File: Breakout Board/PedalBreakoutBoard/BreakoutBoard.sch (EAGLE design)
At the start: 7 parts, among them J1 POWER_JACK, U1 ES_DAISY_SEED_REV4, X1 5566-8, X2 5566-6

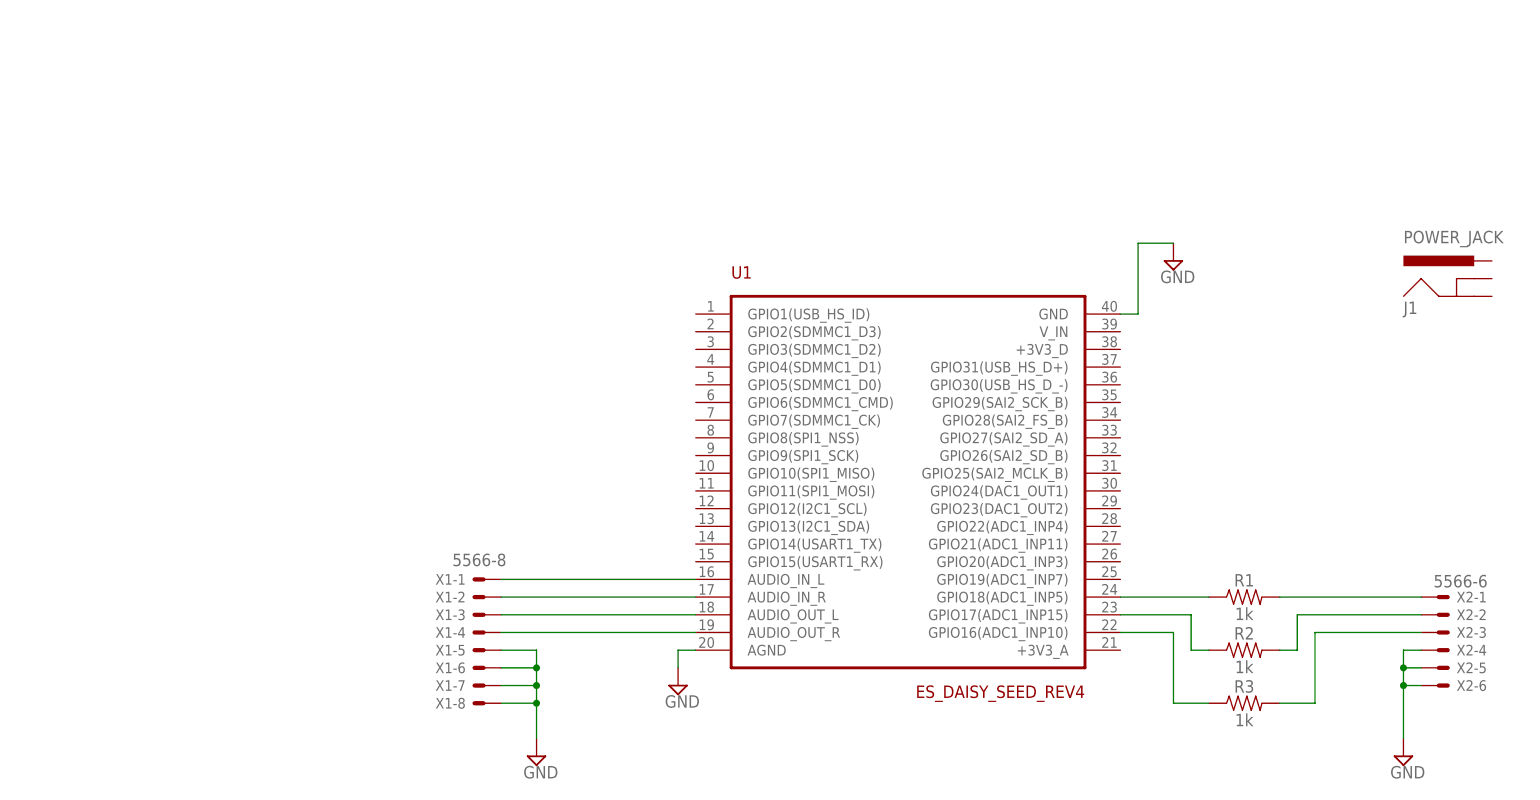
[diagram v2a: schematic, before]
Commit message: DP-16 - Add SPST molex
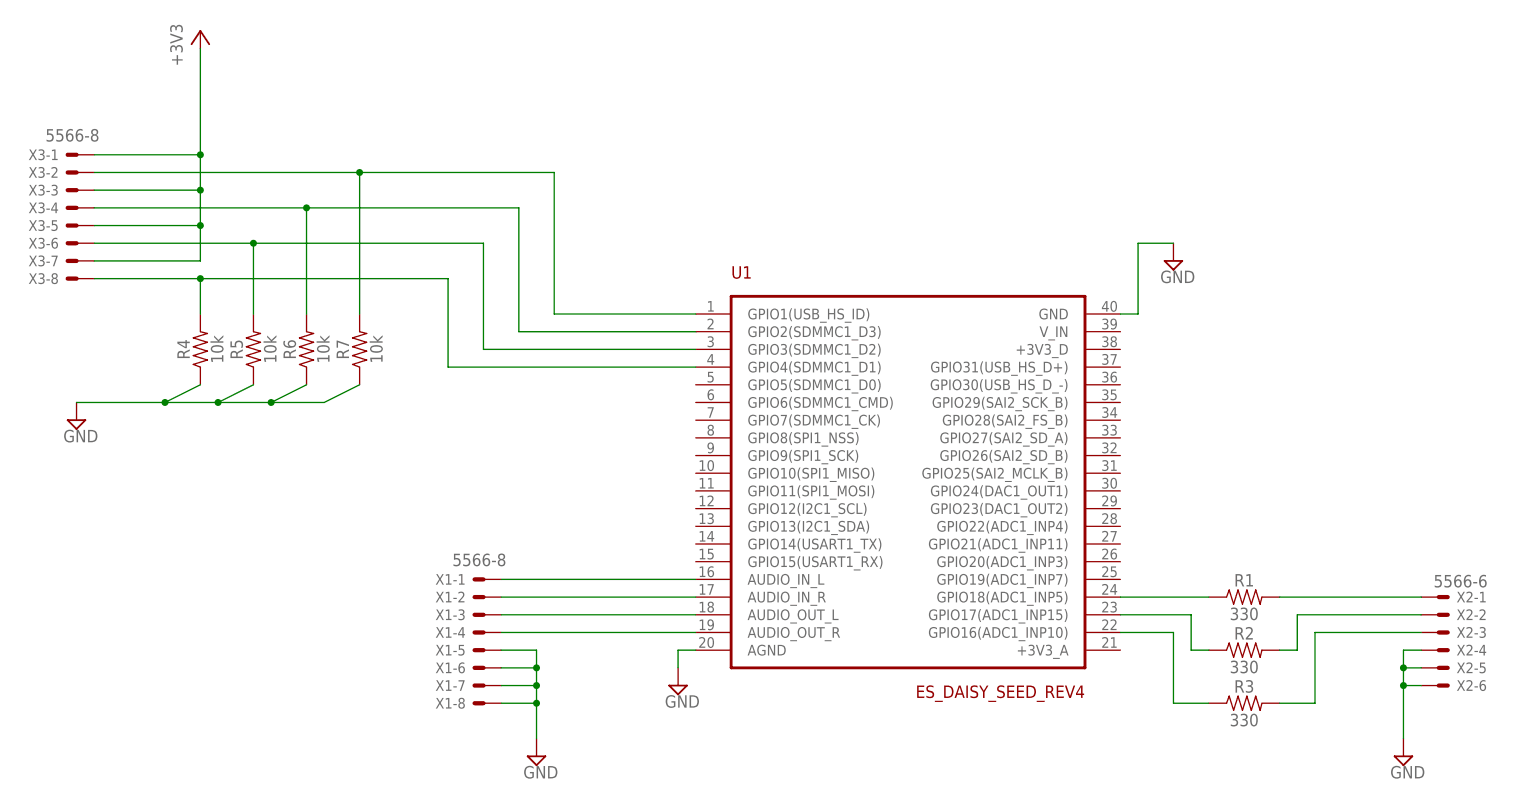
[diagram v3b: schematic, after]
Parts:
- removed J1: POWER_JACK, SparkFun-Connectors:POWER_JACK
- added R4, R5, R6, R7: 10k, SparkFun-Resistors:10KOHM-HORIZ-1/4W-5%
- added X3: 5566-8, con-molex:5566-8
- R1, R2, R3: value 1k -> 330; device SparkFun-Resistors:1KOHM-HORIZ-1/4W-5% -> SparkFun-Resistors:330OHM-HORIZ-1/10W-5%
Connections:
- new net +3V3: X3-1.S, X3-3.S, X3-5.S, X3-7.S
- new net SPST1: R7.2, U1.GPIO1(USB_HS_ID), X3-2.S
- new net SPST2: R6.2, U1.GPIO2(SDMMC1_D3), X3-4.S
- new net SPST3: R5.2, U1.GPIO3(SDMMC1_D2), X3-6.S
- new net SPST4: R4.2, U1.GPIO4(SDMMC1_D1), X3-8.S
- net GND: now also R4.1, R5.1, R6.1, R7.1

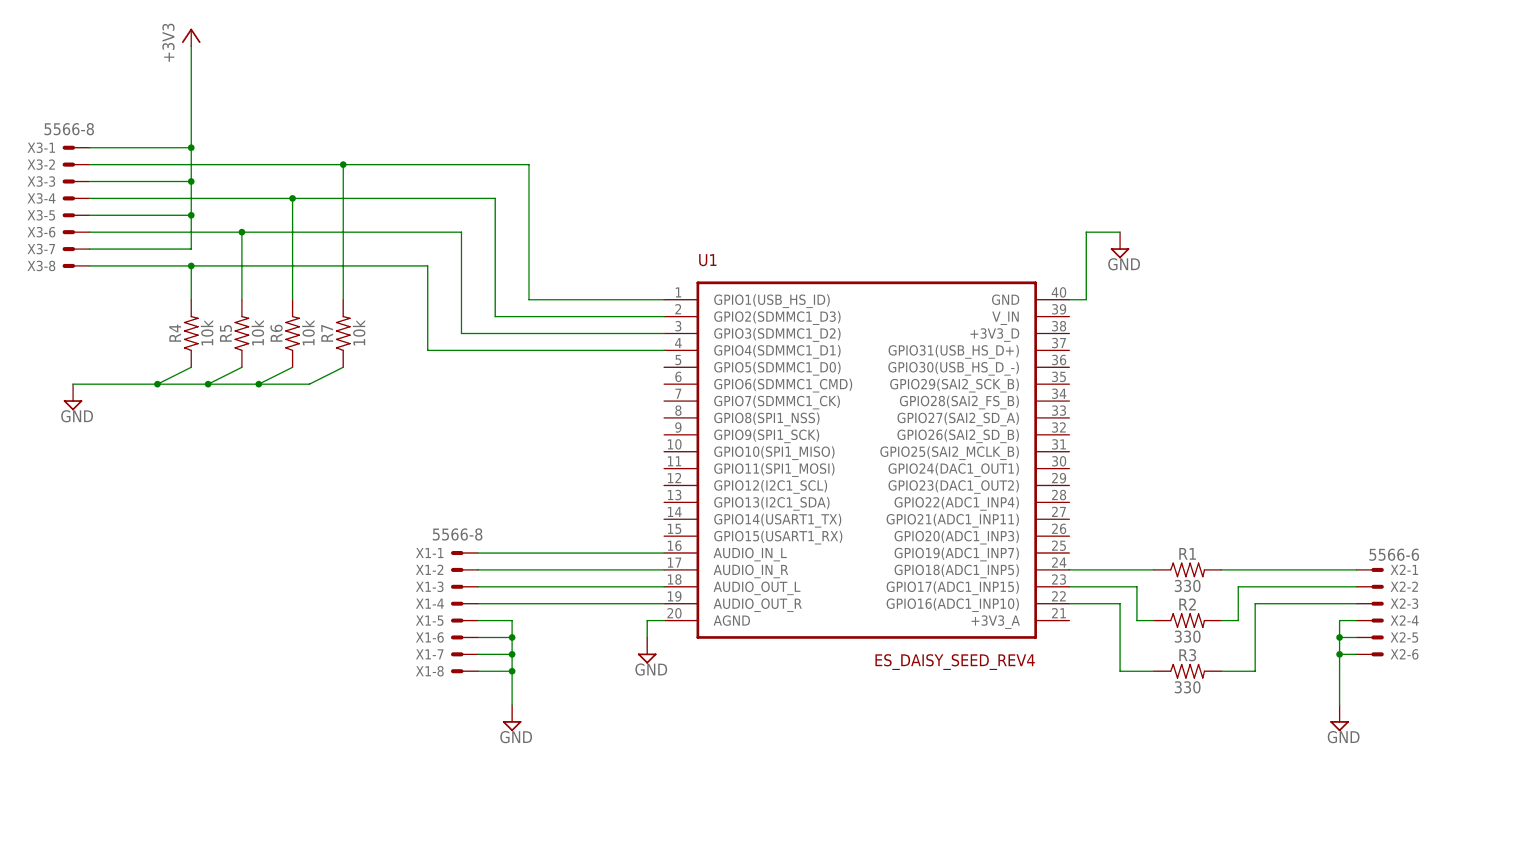
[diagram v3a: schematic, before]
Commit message: DP-16 - Change molex connectors to through holes
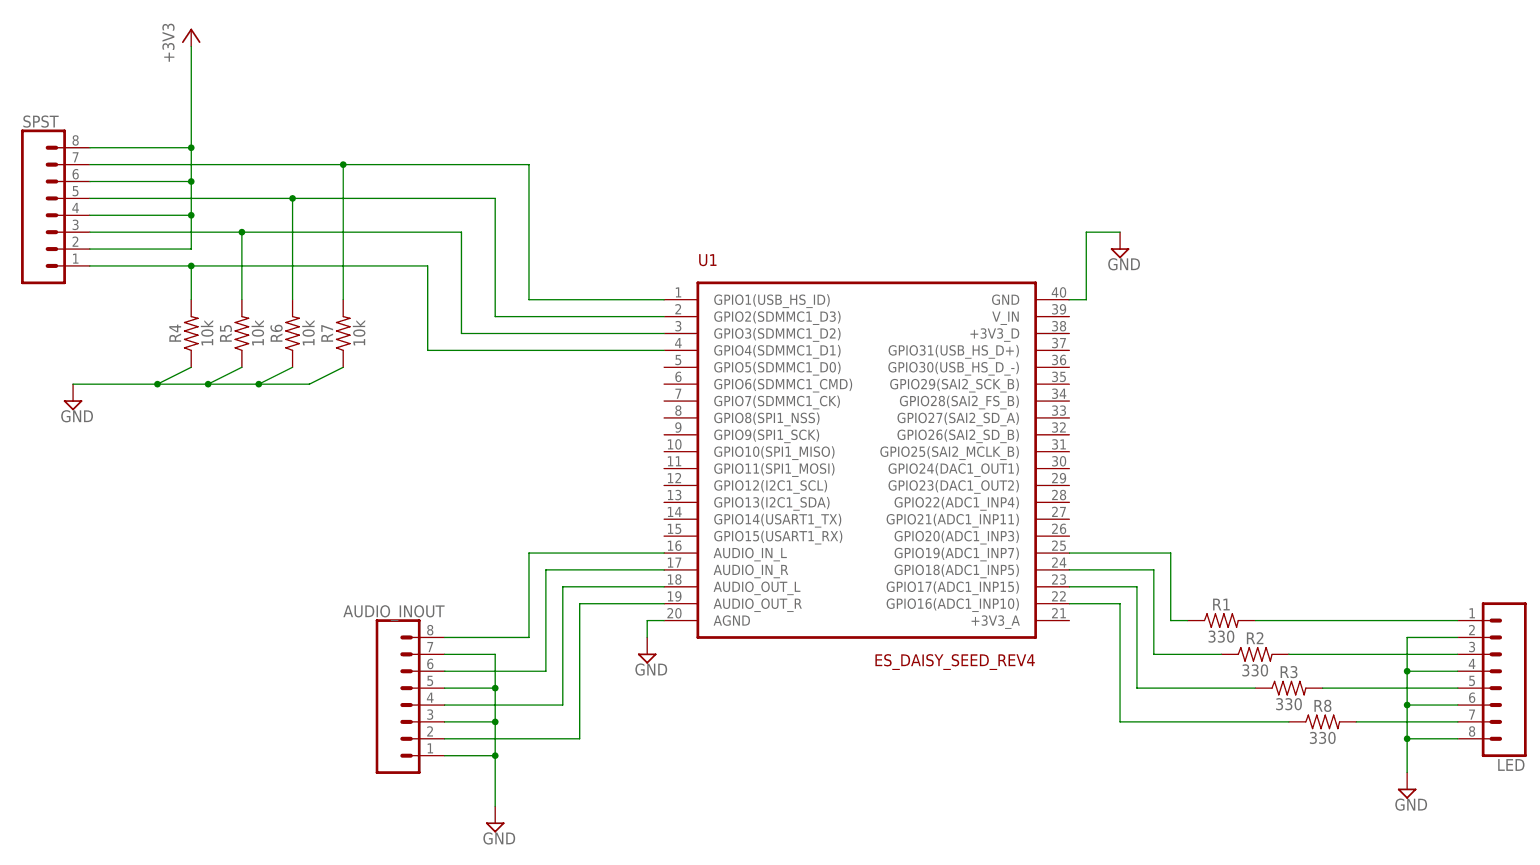
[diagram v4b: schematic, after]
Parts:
- removed X1, X3: 5566-8, con-molex:5566-8
- removed X2: 5566-6, con-molex:5566-6
- added AUDIO_INOUT, LED, SPST: (no value), SparkFun-Connectors:CONN_08"
- added R8: 330, SparkFun-Resistors:330OHM-HORIZ-1/10W-5%
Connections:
- new net N$11: R3.1, U1.GPIO17(ADC1_INP15)
- new net N$12: R8.1, U1.GPIO16(ADC1_INP10)
- net +3V3: now also SPST.2, SPST.4, SPST.6, SPST.8; no longer X3-1.S, X3-3.S, X3-5.S, X3-7.S
- net GND: now also AUDIO_INOUT.1, AUDIO_INOUT.3, AUDIO_INOUT.5, AUDIO_INOUT.7, LED.2, LED.4, LED.6, LED.8; no longer X1-5.S, X1-6.S, X1-7.S, X1-8.S, X2-4.S, X2-5.S, X2-6.S
- net N$1: now also AUDIO_INOUT.8; no longer X1-1.S
- net N$10: now also R2.1, U1.GPIO18(ADC1_INP5); no longer R3.2, X2-3.S
- net N$2: now also AUDIO_INOUT.6; no longer X1-2.S
- net N$3: now also AUDIO_INOUT.4; no longer X1-3.S
- net N$4: now also AUDIO_INOUT.2; no longer X1-4.S
- net N$5: now also LED.1, R1.2; no longer R1.1, U1.GPIO18(ADC1_INP5)
- net N$6: now also LED.3, R2.2; no longer R2.1, U1.GPIO17(ADC1_INP15)
- net N$7: now also LED.5, R3.2; no longer R3.1, U1.GPIO16(ADC1_INP10)
- net N$8: now also LED.7, R8.2; no longer R1.2, X2-1.S
- net N$9: now also R1.1, U1.GPIO19(ADC1_INP7); no longer R2.2, X2-2.S
- net SPST1: now also SPST.7; no longer X3-2.S
- net SPST2: now also SPST.5; no longer X3-4.S
- net SPST3: now also SPST.3; no longer X3-6.S
- net SPST4: now also SPST.1; no longer X3-8.S
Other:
- moved on the sheet: R1, R2, R3

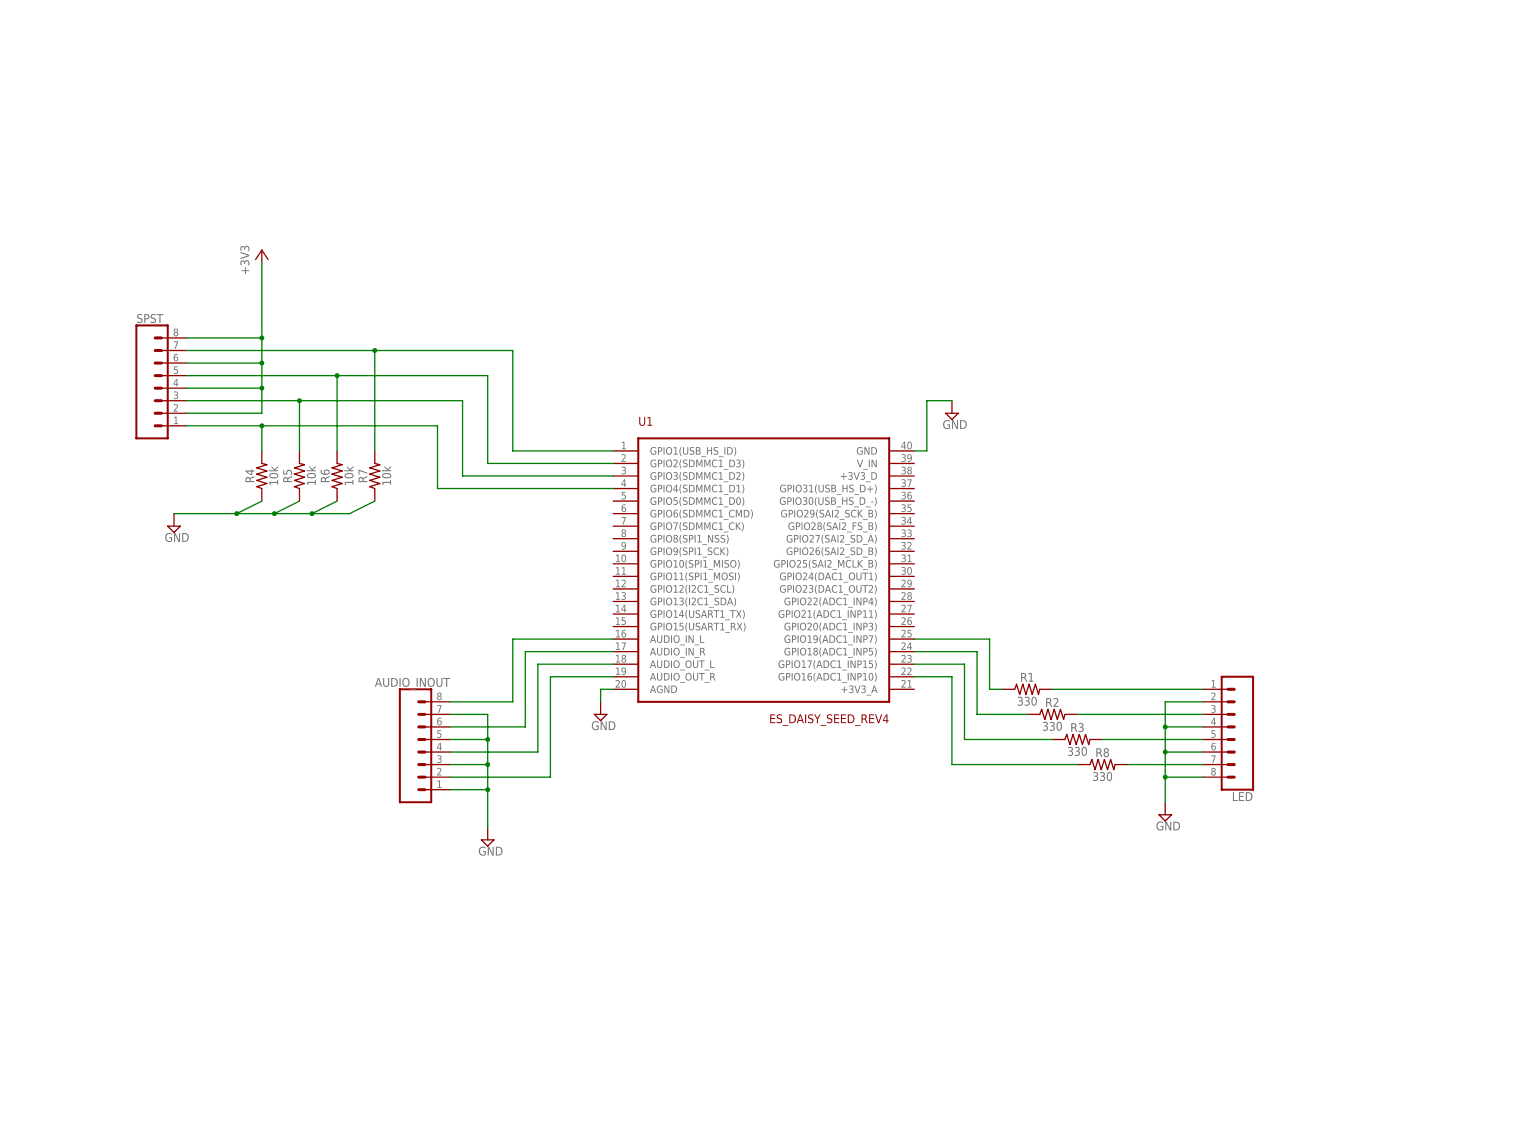
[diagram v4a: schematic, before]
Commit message: DP-16 - Move connections into groups
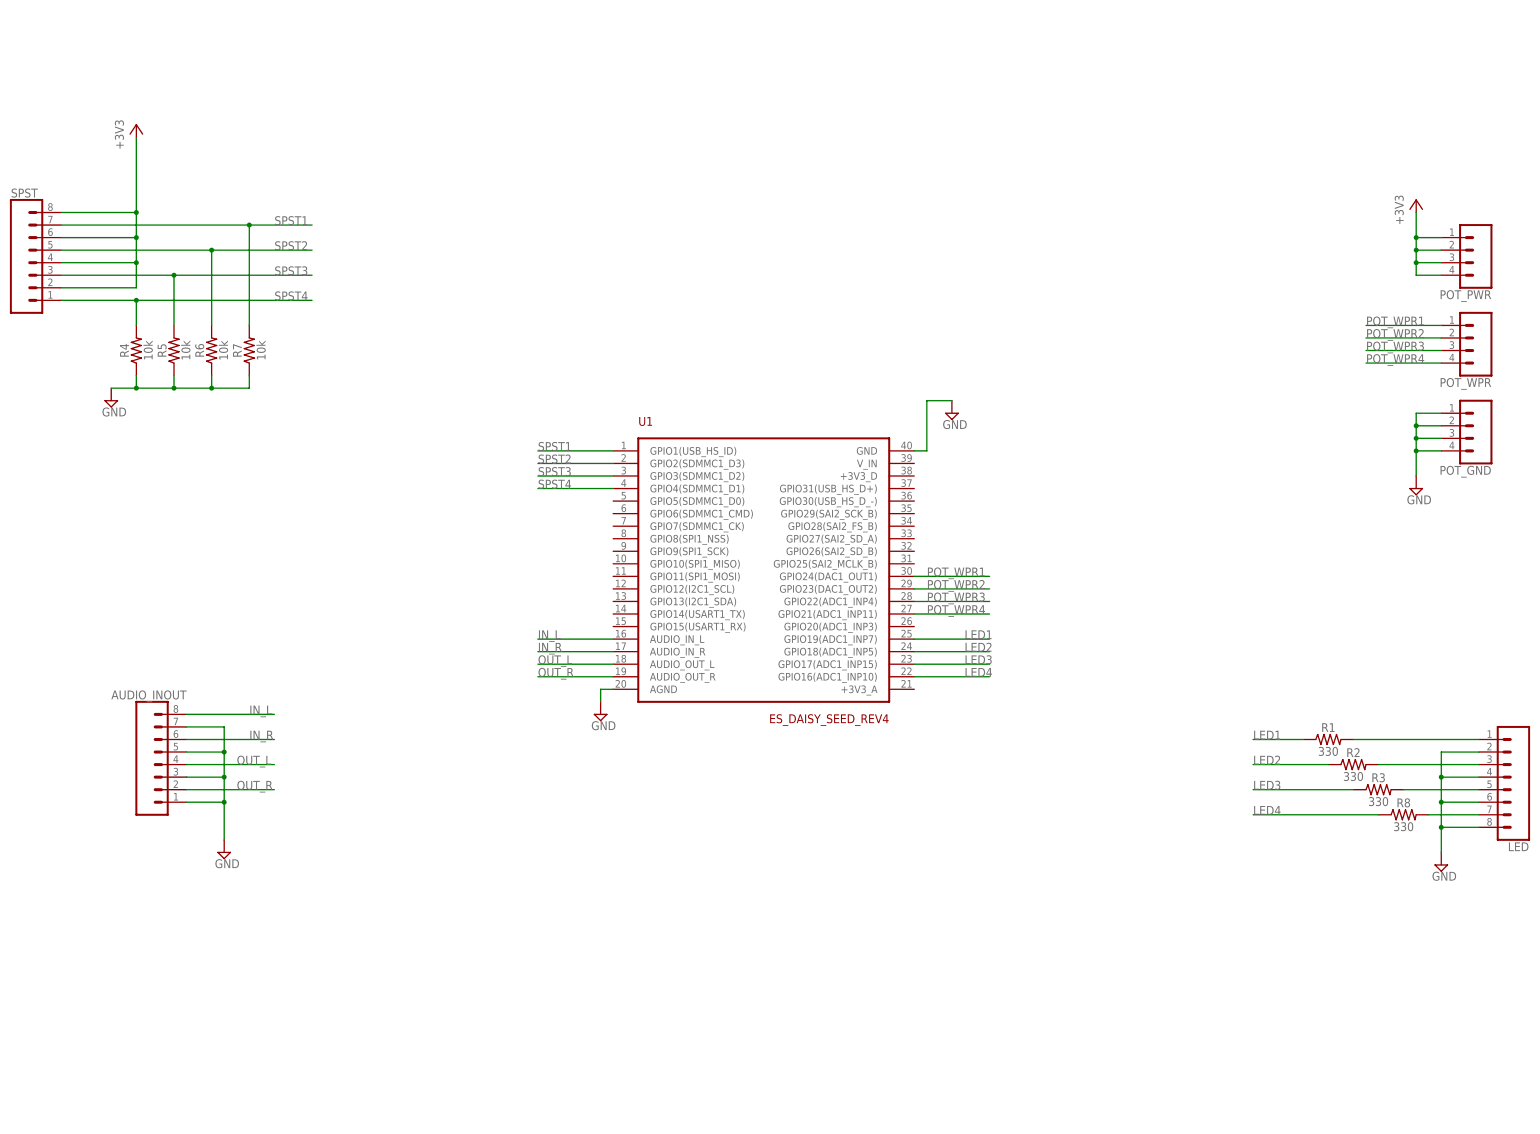
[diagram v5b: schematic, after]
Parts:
- added POT_GND, POT_PWR, POT_WPR: (no value), SparkFun-Connectors:CONN_04
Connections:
- net N$1 renamed IN_L
- net N$10 renamed LED2
- net N$11 renamed LED3
- net N$12 renamed LED4
- net N$2 renamed IN_R
- net N$3 renamed OUT_L
- net N$4 renamed OUT_R
- net N$9 renamed LED1
- new net POT_WPR1: POT_WPR.1, U1.GPIO24(DAC1_OUT1)
- new net POT_WPR2: POT_WPR.2, U1.GPIO23(DAC1_OUT2)
- new net POT_WPR3: POT_WPR.3, U1.GPIO22(ADC1_INP4)
- new net POT_WPR4: POT_WPR.4, U1.GPIO21(ADC1_INP11)
- net +3V3: now also POT_PWR.1, POT_PWR.2, POT_PWR.3, POT_PWR.4
- net GND: now also POT_GND.1, POT_GND.2, POT_GND.3, POT_GND.4
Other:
- moved on the sheet: AUDIO_INOUT, LED, R1, R2, R3, R4, R5, R6, R7, R8, SPST
